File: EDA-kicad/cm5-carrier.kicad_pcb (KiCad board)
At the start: 6 copper layers, 82 x 155 mm, 132 parts, among them J1 USBC-4-0-CX90MW9-24P1, J2 SIM-G85D1160022HHR, J3 FINGER, J4 SJ2-35894B-SMT-TR, SW1 EG25-switch-CSS-1210MC, SW2 MIC-switch-CSS-1210MC, SW3 CAM-switch-CSS-1210MC, SW4 PROG, SW5 VOL-, SW6 VOL+, SW7 POW, U1 EG25GGC-128-SGNS, U10 22V-boost-AP3032KTR-G1, U11 MP3429GL-Z, U12 FPC15pin-1mm-pitch-F52Q-1A7H1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, U13 Flash-LED-Lumiled, U4 CODEC-TLV320AIC3204IRHBR, U7 BQ25792RQMR, U9 BAT-CONNECTOR-FLTS22WR00

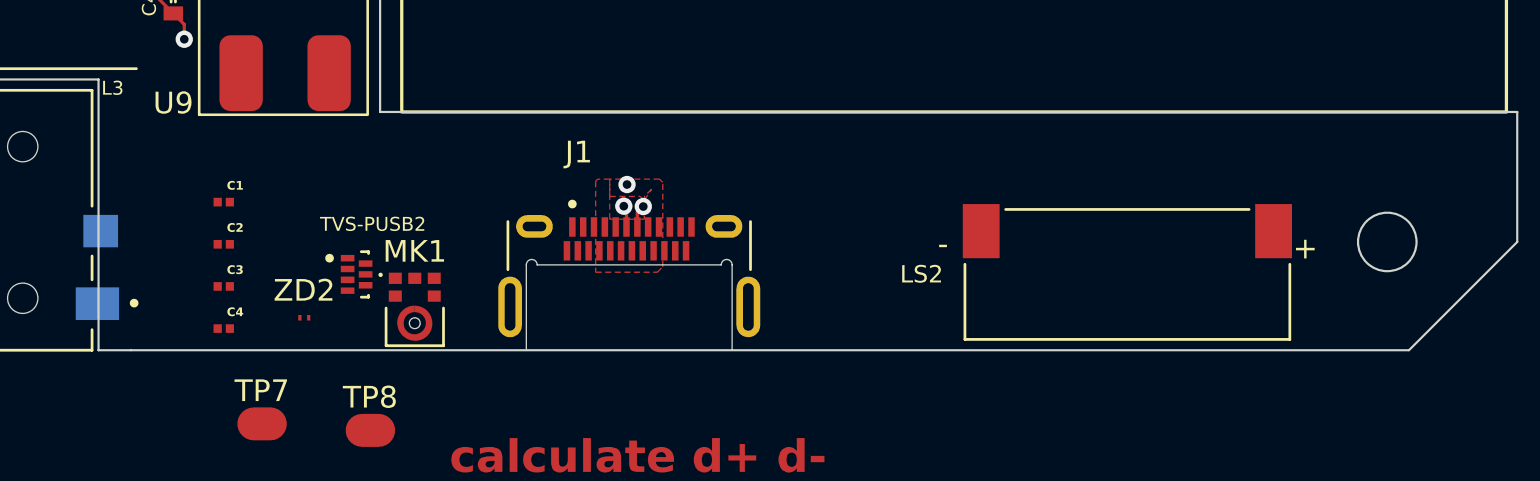
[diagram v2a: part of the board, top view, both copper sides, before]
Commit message: fix USB C cutout
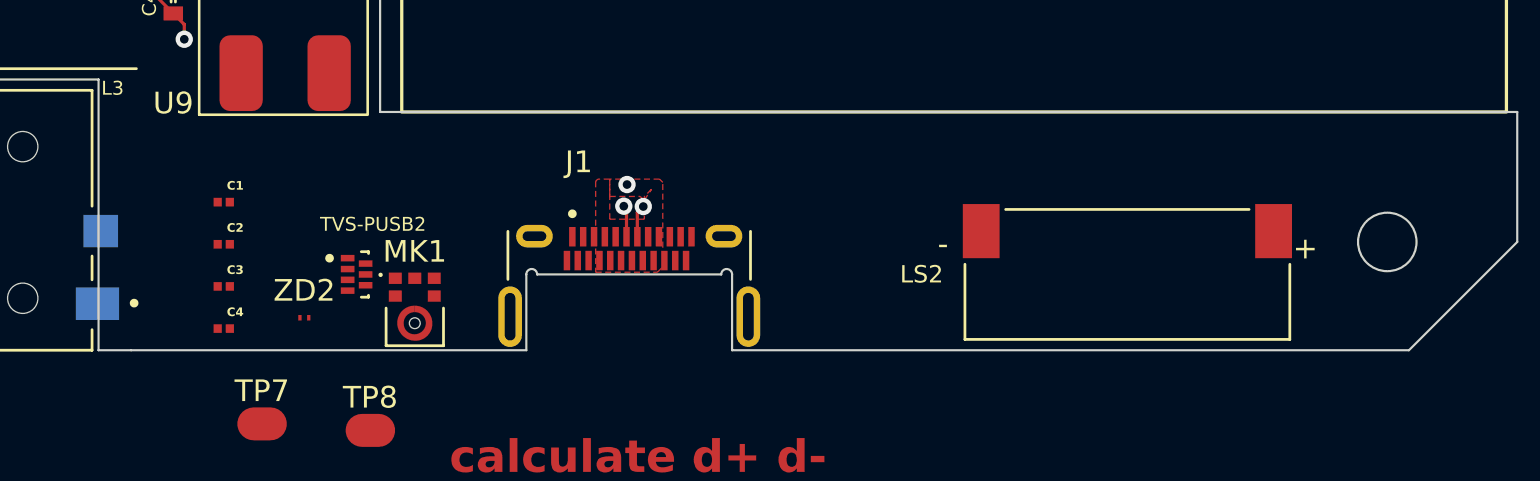
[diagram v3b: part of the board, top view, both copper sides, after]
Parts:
- moved J1 0.45 mm to (95.0, 184.4)
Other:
- outline, holes or cut-outs redrawn
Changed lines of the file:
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@@
 	(footprint "SPIRIT-footprints:USB-4-0-HIROSE_CX90MW9-24P1"
 		(layer "F.Cu")
-		(at 95 184)
+		(at 95 184.45)
 		(property "Reference" "J1"
 			(at -2.325 -7.135 0)
@@
 		(fp_line
 			(start -4.75 -1.94)
-			(end -4.75 2)
+			(end -4.75 1.81)
 			(stroke
 				(width 0.01)
 				(type solid)
 			)
-			(layer "Edge.Cuts")
+			(layer "Dwgs.User")
 		)
 		(fp_line
-			(start -4.75 2)
-			(end 4.75 2)
+			(start -4.75 1.81)
+			(end 4.75 1.81)
 			(stroke
 				(width 0.01)
 				(type solid)
 			)
-			(layer "Edge.Cuts")
+			(layer "Dwgs.User")
 		)
 		(fp_line
@@
 				(type solid)
 			)
-			(layer "Edge.Cuts")
+			(layer "Dwgs.User")
 		)
 		(fp_line
-			(start 4.75 2)
+			(start 4.75 1.81)
 			(end 4.75 -1.94)
 			(stroke
@@
 				(type solid)
 			)
-			(layer "Edge.Cuts")
+			(layer "Dwgs.User")
 		)
 		(fp_arc
@@
 				(type solid)
 			)
-			(layer "Edge.Cuts")
+			(layer "Dwgs.User")
 		)
 		(fp_arc
@@
 				(type solid)
 			)
-			(layer "Edge.Cuts")
+			(layer "Dwgs.User")
 		)
 		(fp_arc
@@
 				(type solid)
 			)
-			(layer "Edge.Cuts")
+			(layer "Dwgs.User")
 		)
 		(fp_arc
@@
 				(type solid)
 			)
-			(layer "Edge.Cuts")
+			(layer "Dwgs.User")
 		)
 		(fp_line
@@
 		)
 		(fp_line
-			(start -5.6 1.81)
-			(end 5.6 1.81)
+			(start -5.6 4.06)
+			(end -5.6 1.81)
 			(stroke
 				(width 0.127)
@@
 		)
 		(fp_line
-			(start -5.6 4.06)
-			(end -5.6 1.81)
+			(start -5.6 6.1)
+			(end 8.75 6.1)
 			(stroke
 				(width 0.127)
@@
 		(layer "Edge.Cuts")
 	)
+	(gr_arc
+		(start 99.25 182.5)
+		(mid 99.5 182.25)
+		(end 99.75 182.5)
+		(stroke
+			(width 0.1)
+			(type default)
+		)
+		(layer "Edge.Cuts")
+	)
 	(gr_line
 		(start 70.5 173.5)
@@
 	(gr_line
 		(start 131 186)
-		(end 72 186)
+		(end 99.75 186)
 		(stroke
 			(width 0.1)
@@
 	)
 	(gr_line
+		(start 90.25 186)
+		(end 90.25 182.5)
+		(stroke
+			(width 0.1)
+			(type default)
+		)
+		(layer "Edge.Cuts")
+	)
+	(gr_line
 		(start 54.5 66.25)
 		(end 54.5 44.25)
@@
 		(layer "Edge.Cuts")
 	)
+	(gr_arc
+		(start 90.25 182.5)
+		(mid 90.5 182.25)
+		(end 90.75 182.5)
+		(stroke
+			(width 0.1)
+			(type default)
+		)
+		(layer "Edge.Cuts")
+	)
 	(gr_circle
 		(center 58.5 37.3)
@@
 	)
 	(gr_line
+		(start 90.25 186)
+		(end 72 186)
+		(stroke
+			(width 0.1)
+			(type solid)
+		)
+		(layer "Edge.Cuts")
+	)
+	(gr_line
 		(start 136 181)
 		(end 131 186)
@@
 	)
 	(gr_line
+		(start 99.75 186)
+		(end 99.75 182.5)
+		(stroke
+			(width 0.1)
+			(type default)
+		)
+		(layer "Edge.Cuts")
+	)
+	(gr_line
 		(start 59 186)
 		(end 54 181)
@@
 	)
 	(gr_line
+		(start 99.25 182.5)
+		(end 90.75 182.5)
+		(stroke
+			(width 0.1)
+			(type solid)
+		)
+		(layer "Edge.Cuts")
+	)
+	(gr_line
 		(start 54 94)
 		(end 54.5 94)
@@
 			(pts
 				(xy 94.1 179.95) (xy 94.1 178.1) (xy 93.55 178.1) (xy 93.45 178.2) (xy 93.45 182.4) (xy 96.3 182.4)
-				(xy 96.55 182.15) (xy 96.55 178.25) (xy 96.4 178.1) (xy 94.1 178.1) (xy 94.1 178.9) (xy 94.1 178.9)
-				(xy 95.5 178.9) (xy 95.7 179.066666) (xy 96.031817 178.568183) (xy 95.7 178.9) (xy 95.7 179.95)
+				(xy 96.55 182.15) (xy 96.55 178.25) (xy 96.4 178.1) (xy 94.1 178.1) (xy 94.1 178.9) (xy 95.5 178.9)
+				(xy 95.7 179.066666) (xy 96.031817 178.568183) (xy 95.7 178.9) (xy 95.7 179.95)
 			)
 		)
@@
 			(pts
 				(xy 95.5 177.739734) (xy 77.85 177.65) (xy 73.35 173.25) (xy 68.4 168.415117) (xy 68.4 156.9) (xy 67.2 156.9)
-				(xy 67.2 160.3) (xy 67.2 169.45) (xy 77.4 179.15) (xy 95.5 179.15) (xy 95.5 179.15)
+				(xy 67.2 160.3) (xy 67.2 169.45) (xy 77.4 179.15) (xy 95.5 179.15)
 			)
 		)

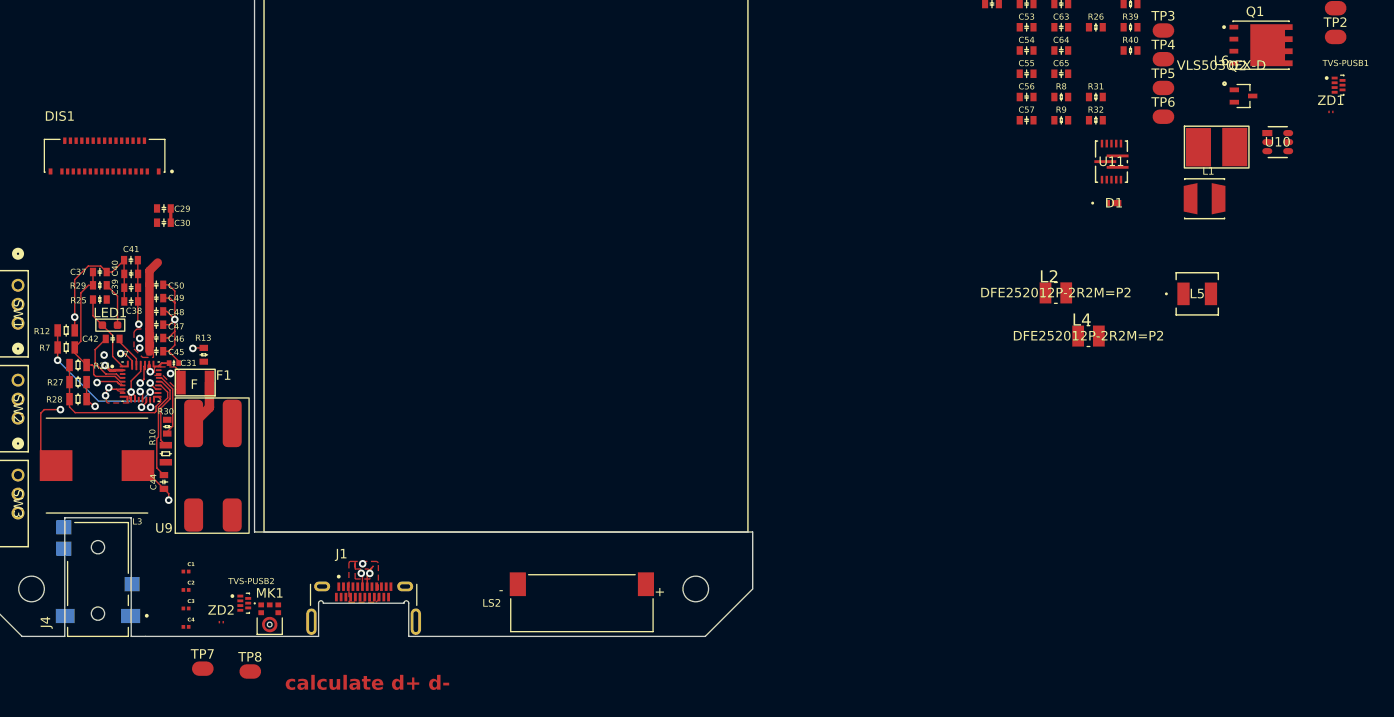
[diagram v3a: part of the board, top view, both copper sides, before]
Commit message: add USB-MUX HD3SS460
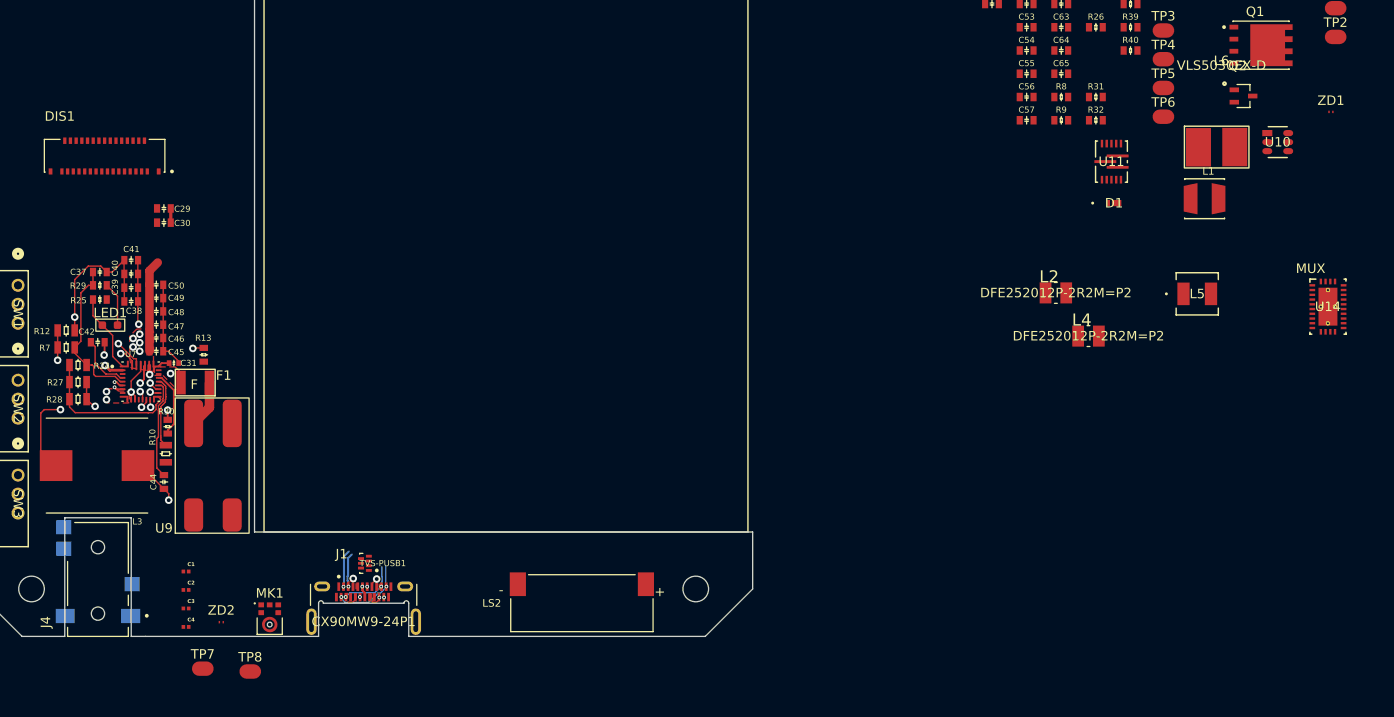
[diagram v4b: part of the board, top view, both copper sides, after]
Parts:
- removed TVS-PUSB2: ~, SPIRIT-footprints:TVS-array-IC_PUSB3AB6Z
- added U14: HD3SS460RHRR, SPIRIT-footprints:USB-MUX-RHR0028A, F.Cu at (196.6, 151.3)
- moved TVS-PUSB1 114.3 mm to (95.1, 178.3), turned to 180 degrees
- moved C42 1.61 mm to (67.0, 155.0)
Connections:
- Module1 pad 78: unconnected-(Module1A-GPIO_VREF(1.8v/3.3v_Input)-Pad78) -> 3V3B
- Module1 pad 80: SCL PMIC -> SCL PWR
- Module1 pad 82: SDA PMIC -> SDA PWR
- U7 pad 14: SCL CH -> SCL PWR
- U7 pad 15: SDA CH -> SDA PWR
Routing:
- net D+: track 43.9 -> 2.20 mm
- net D-: track 42.7 -> 2.34 mm, vias 2 -> 3
- net RX1+: track 0.00 -> 8.00 mm, vias 0 -> 2
- net GND: track 42.9 -> 35.8 mm, vias 4 -> 3
- net RX1-: track 0.00 -> 6.36 mm, vias 0 -> 2
- net TX1+: track 0.00 -> 3.95 mm, vias 0 -> 2
- net TX1-: track 0.00 -> 3.62 mm, vias 0 -> 2
- net Net-(U7-SW1): track 21.9 -> 25.0 mm, vias 2 -> 3
- net SDA PWR: track 0.00 -> 1.13 mm, vias 0 -> 1
- net SDA CH: track 1.13 -> 0.00 mm, vias 1 -> 0
- net 3V3B: track 0.00 -> 1.03 mm, vias 0 -> 1
- net SCL PWR: track 0.00 -> 1.01 mm, vias 0 -> 1
- net SCL CH: track 1.01 -> 0.00 mm, vias 1 -> 0
- net Net-(U7-ILIM_HIZ): track 16.0 -> 16.6 mm
- net Net-(U7-BTST1): track 6.57 -> 5.94 mm
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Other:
- board text removed: "calculate d+ d-"

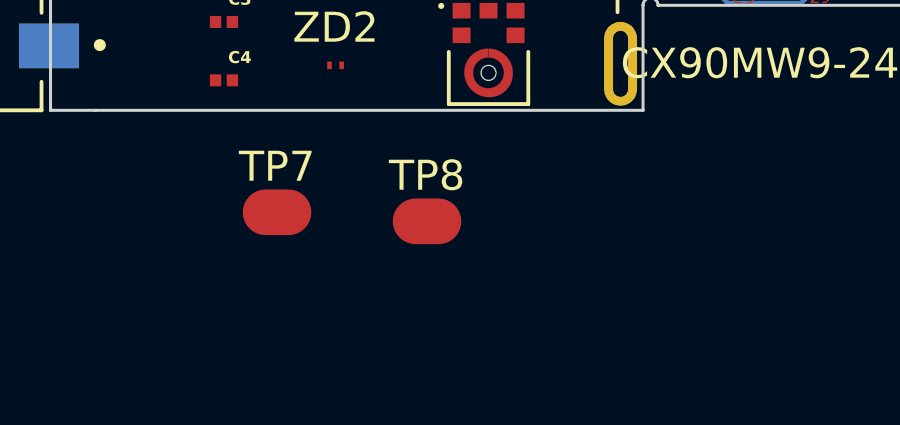
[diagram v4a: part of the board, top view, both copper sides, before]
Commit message: add USB 2 switch
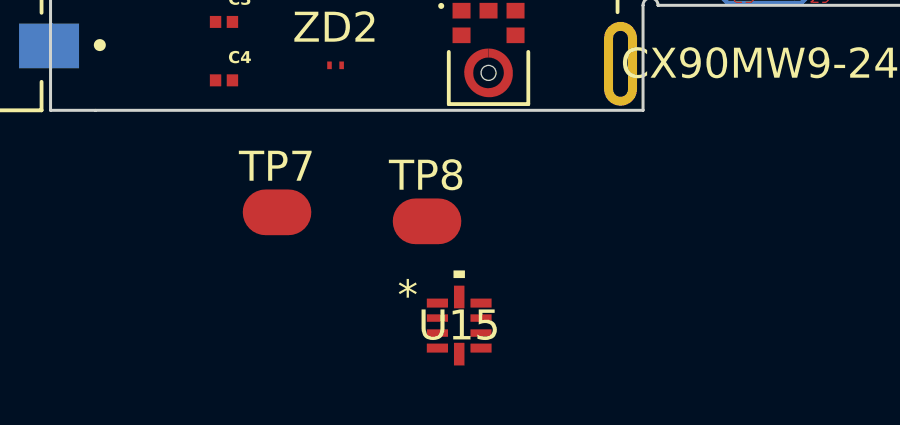
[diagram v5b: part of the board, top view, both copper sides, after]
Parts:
- added U15: USB SWITCH 2CHANNEL TS3USB221AQRSERQ1, SPIRIT-footprints:USB-SWITCH-2CHANNEL-TS3USB221AQRSERQ1, F.Cu at (84.1, 193.2)
